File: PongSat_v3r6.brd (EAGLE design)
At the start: 39 x 39 mm, 34 parts, among them U1 MIC5129 3v3, U2 Micro SD, X1 USB-MICROB, Y1 8MHz

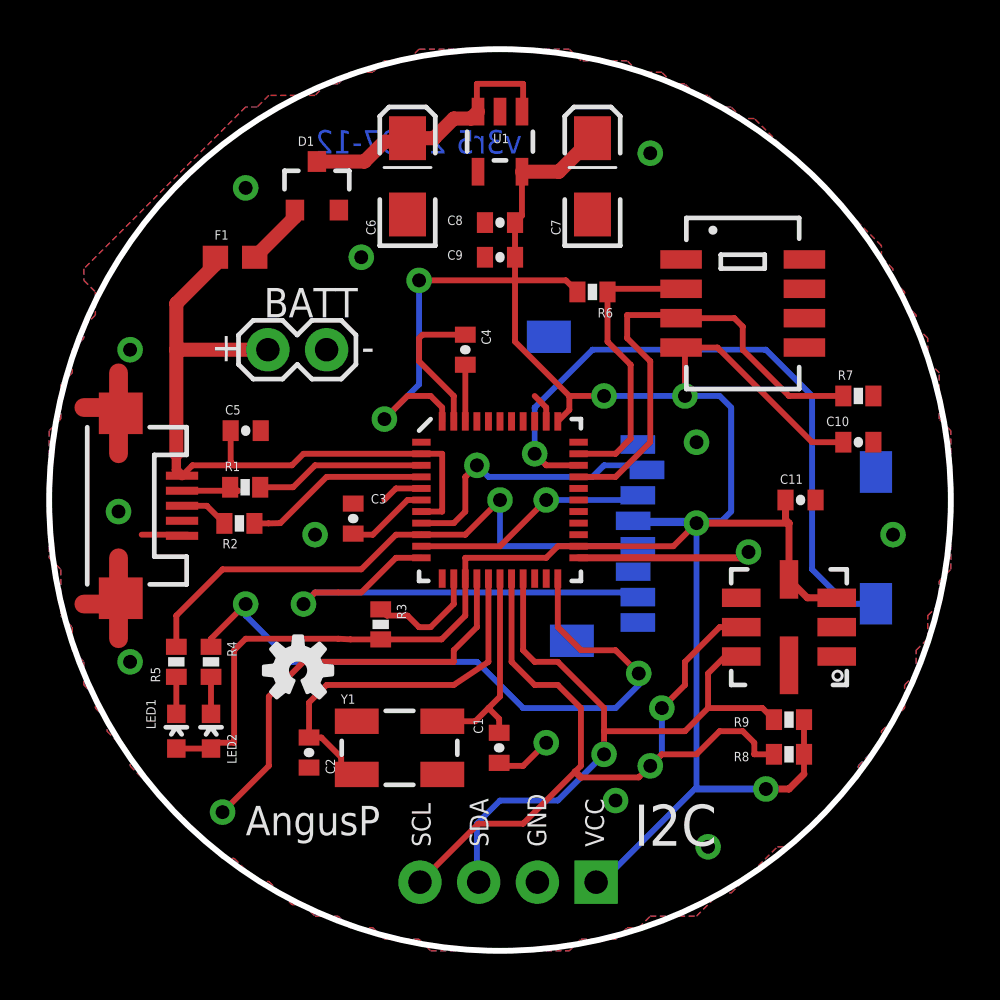
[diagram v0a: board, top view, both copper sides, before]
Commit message: Revision 6
Removed acid traps and improved silkscreen. New rev 6 gerber files as
well. Version 4 will be along soon in the main branch…
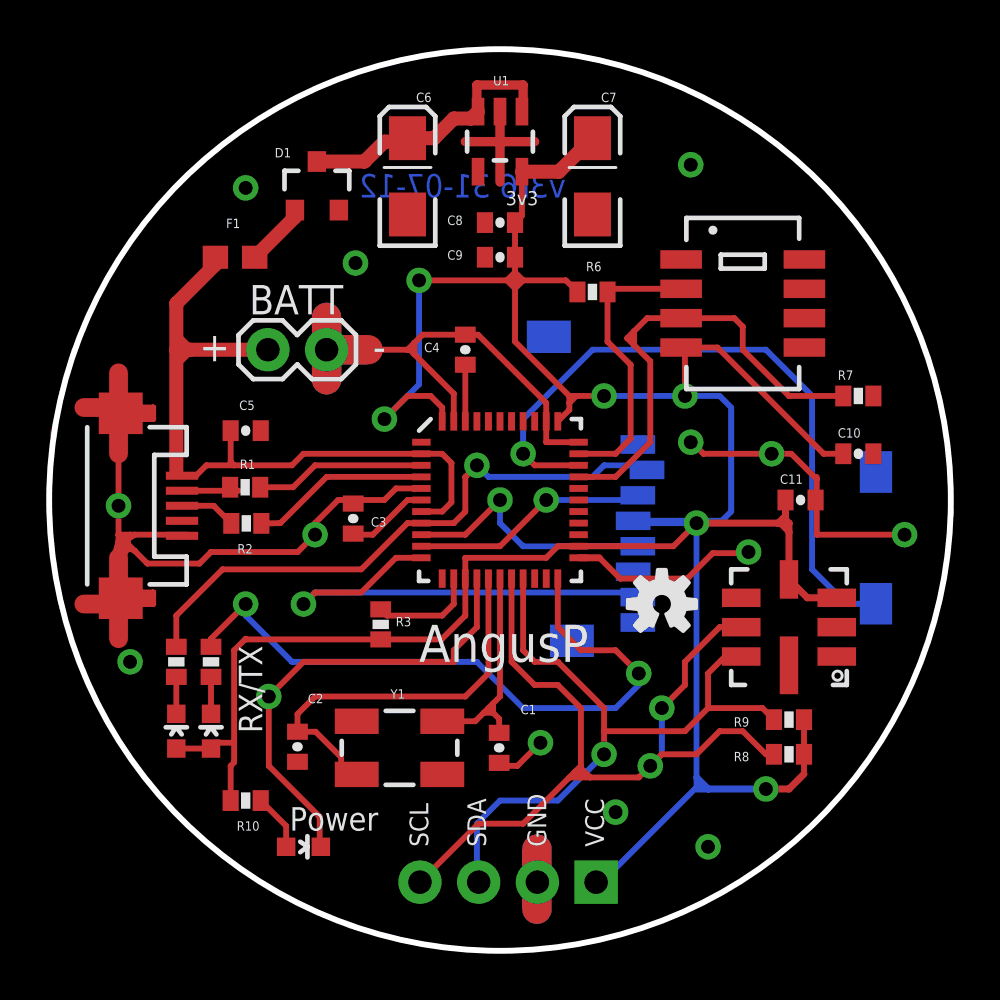
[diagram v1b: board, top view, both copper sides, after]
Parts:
- removed U$1: (no value), SparkFun-Aesthetics:OSHW-LOGO-S
- added LED3: Blue, SparkFun-LED:LED-0603
- added R10: 1K, SparkFun-Passives:0402-RES
- added U$2: OSHW-LOGOS, SparkFun-Aesthetics:OSHW-LOGO-S
- F1: value PTC0603 -> 500mA
- R1, R2: value 220 -> 22
- moved C2 0.56 mm to (10.7, 8.83)
- moved C10 0.50 mm to (35.0, 21.5)
- moved R2 0.30 mm to (8.53, 18.5)
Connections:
- new net N$8: LED3.A, R10.1
- net 3.3V: now also R10.2
- net CS: now also R5.2
- net GND: now also 32U4.33, LED3.C
- net SCK: no longer R5.2
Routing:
- net GND: track 49.2 -> 126.8 mm
- net SCK: track 25.4 -> 11.4 mm
- net CS: track 12.2 -> 25.8 mm
- net 3.3V: track 127.9 -> 134.6 mm
- net UVCC: track 30.8 -> 34.1 mm
- net N$8: track 0.00 -> 2.46 mm
- net SCL: track 37.4 -> 38.7 mm
- net N$1: track 17.0 -> 18.0 mm
- net N$2: track 9.46 -> 10.3 mm
- net CD: track 28.8 -> 29.6 mm
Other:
- board text added: "3v3"
- board text added: "Power"
- board text added: "RX/TX"
- board text added: "v3r6 31-07-12"
- board text removed: "I2C"
- board text removed: "v3r5 29-07-12"
